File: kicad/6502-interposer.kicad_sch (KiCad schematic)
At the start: 6 parts, among them J1 Conn_02x16_Odd_Even_MountingP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, J2 Conn_02x16_Odd_Even_MountingP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, J3 Conn_02x09_Odd_Even, U1 65CE02

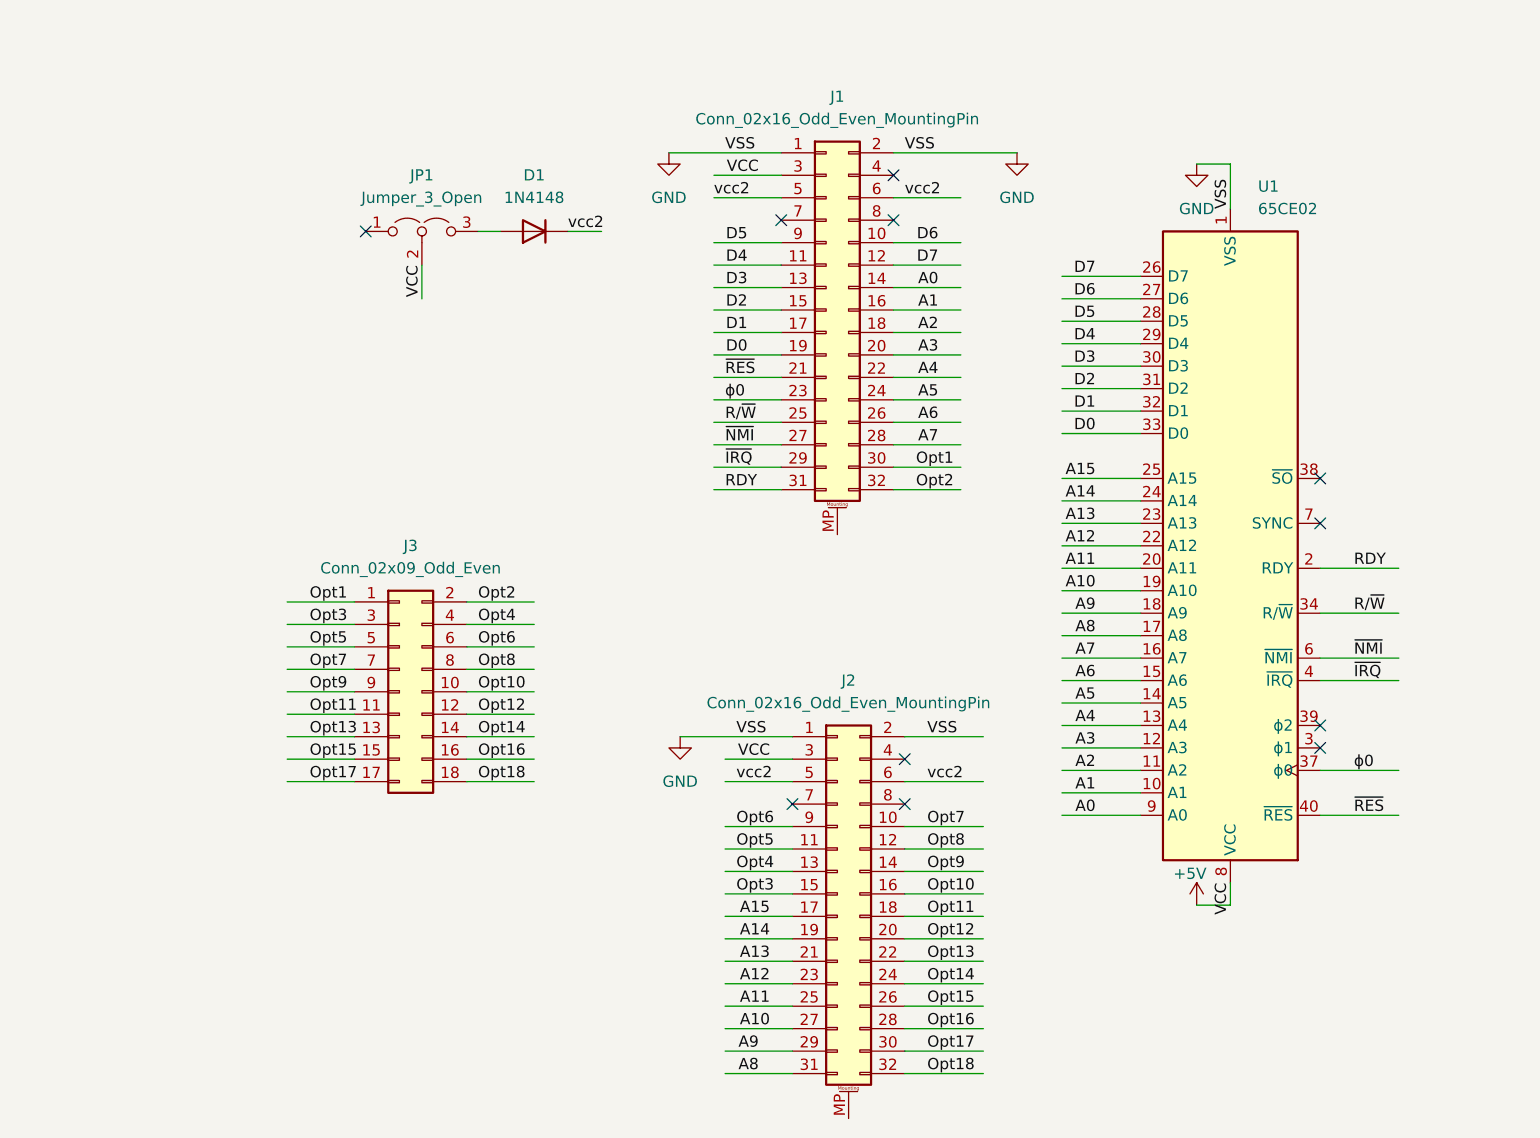
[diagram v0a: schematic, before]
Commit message: version 1.5
Fix board labelling issues. Fix Numbering issues.
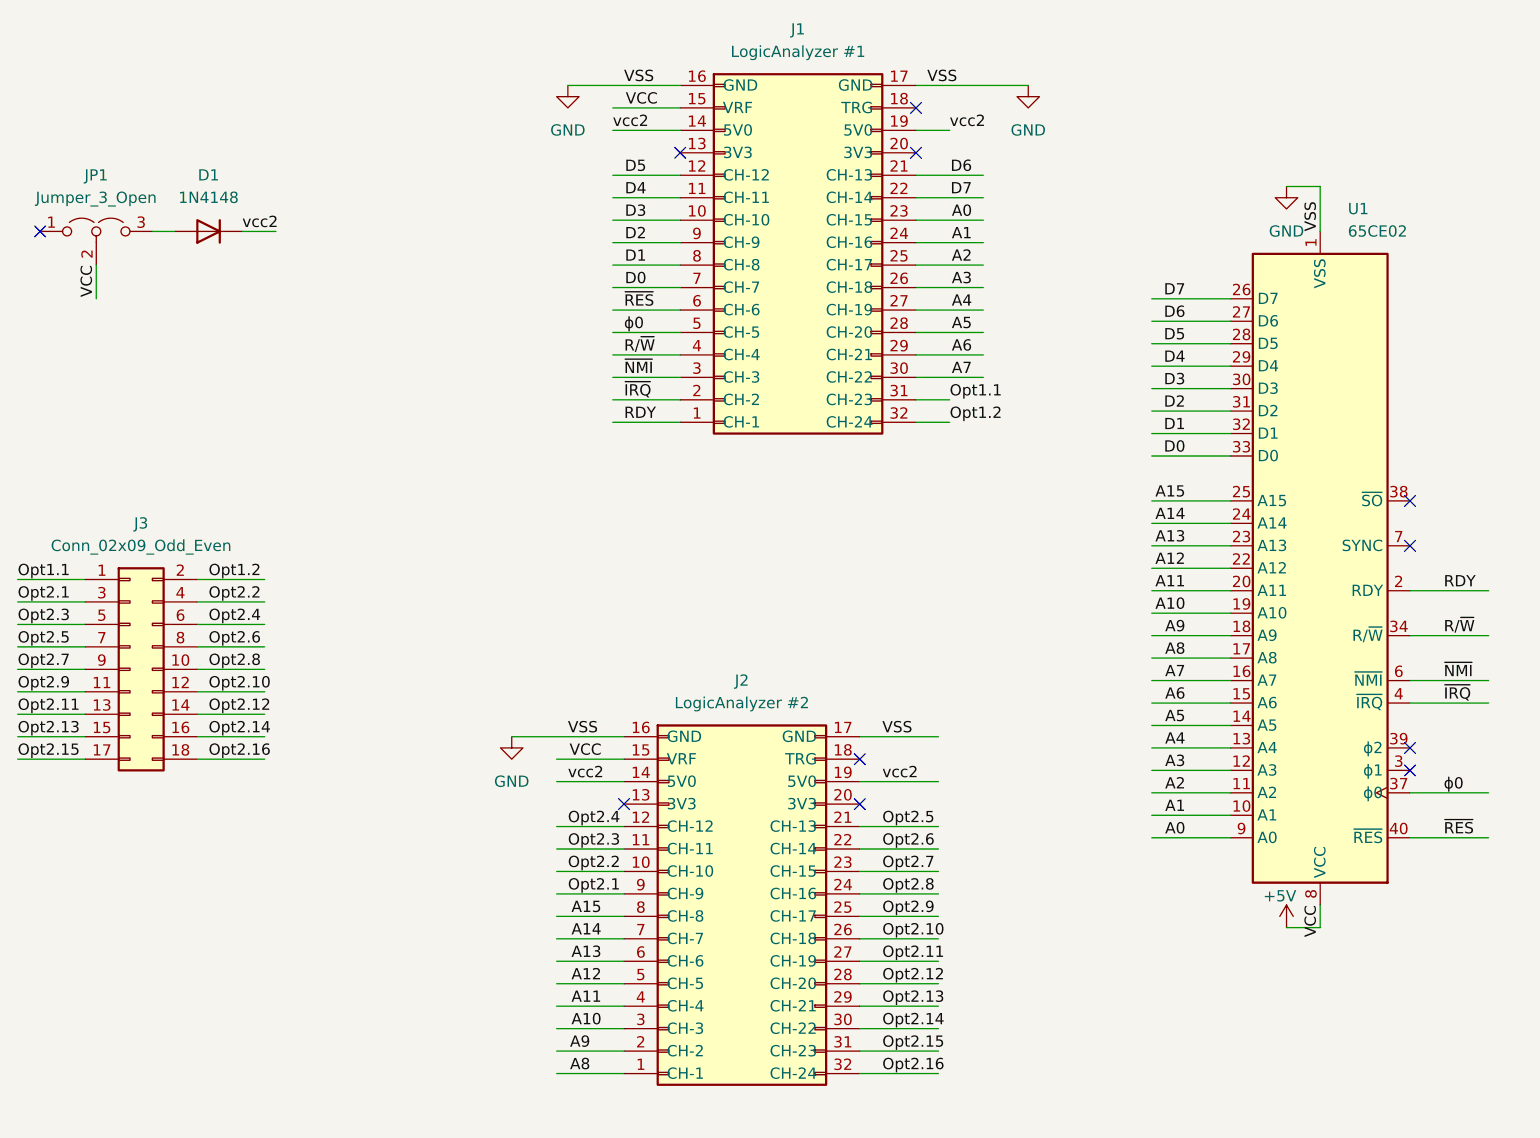
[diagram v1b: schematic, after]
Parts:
- J1: value Conn_02x16_Odd_Even_MountingPin -> LogicAnalyzer #1
- J2: value Conn_02x16_Odd_Even_MountingPin -> LogicAnalyzer #2; symbol Connector_Generic_MountingPin:Conn_02x16_Odd_Even_MountingPin -> LocalLibrary:Dr_Gusman's_Logic_Analyzer_Pinout
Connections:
- net +5V: now also J1.15 (VRF), J2.15 (VRF); no longer J1.3 (Pin_3), J2.3 (Pin_3)
- net A0: now also J1.23 (CH-15); no longer J1.14 (Pin_14)
- net A1: now also J1.24 (CH-16); no longer J1.16 (Pin_16)
- net A10: now also J2.3 (CH-3); no longer J2.27 (Pin_27)
- net A11: now also J2.4 (CH-4); no longer J2.25 (Pin_25)
- net A12: now also J2.5 (CH-5); no longer J2.23 (Pin_23)
- net A13: now also J2.6 (CH-6); no longer J2.21 (Pin_21)
- net A14: now also J2.7 (CH-7); no longer J2.19 (Pin_19)
- net A15: now also J2.8 (CH-8); no longer J2.17 (Pin_17)
- net A2: now also J1.25 (CH-17); no longer J1.18 (Pin_18)
- net A3: now also J1.26 (CH-18); no longer J1.20 (Pin_20)
- net A4: now also J1.27 (CH-19); no longer J1.22 (Pin_22)
- net A5: now also J1.28 (CH-20); no longer J1.24 (Pin_24)
- net A6: now also J1.29 (CH-21); no longer J1.26 (Pin_26)
- net A7: now also J1.30 (CH-22); no longer J1.28 (Pin_28)
- net A8: now also J2.1 (CH-1); no longer J2.31 (Pin_31)
- net A9: now also J2.2 (CH-2); no longer J2.29 (Pin_29)
- net D0: now also J1.7 (CH-7); no longer J1.19 (Pin_19)
- net D1: now also J1.8 (CH-8); no longer J1.17 (Pin_17)
- net D2: now also J1.9 (CH-9); no longer J1.15 (Pin_15)
- net D3: now also J1.10 (CH-10); no longer J1.13 (Pin_13)
- net D5: now also J1.12 (CH-12); no longer J1.9 (Pin_9)
- net D6: now also J1.21 (CH-13); no longer J1.10 (Pin_10)
- net D7: now also J1.22 (CH-14); no longer J1.12 (Pin_12)
- net GND: now also J1.16 (GND), J1.17 (GND), J2.16 (GND), J2.17 (GND); no longer J1.1 (Pin_1), J1.2 (Pin_2), J2.1 (Pin_1), J2.2 (Pin_2)
- net R/~{W}: now also J1.4 (CH-4); no longer J1.25 (Pin_25)
- net RDY: now also J1.1 (CH-1); no longer J1.31 (Pin_31)
- net vcc2: now also J1.14 (5V0), J1.19 (5V0), J2.14 (5V0), J2.19 (5V0); no longer J1.5 (Pin_5), J1.6 (Pin_6), J2.5 (Pin_5), J2.6 (Pin_6)
- net ~{IRQ}: now also J1.2 (CH-2); no longer J1.29 (Pin_29)
- net ~{NMI}: now also J1.3 (CH-3); no longer J1.27 (Pin_27)
- net ~{RES}: now also J1.6 (CH-6); no longer J1.21 (Pin_21)
- net ϕ0: now also J1.5 (CH-5); no longer J1.23 (Pin_23)
- net Opt1 renamed Opt1.1
- net Opt1.1: now also J1.31 (CH-23); no longer J1.30 (Pin_30)
- net Opt10 renamed Opt2.8
- net Opt2.8: now also J2.24 (CH-16); no longer J2.16 (Pin_16)
- net Opt11: no longer names the net of J2.18 (TRG)
- net Opt11: no longer J3.11 (Pin_11)
- net Opt12: no longer names the net of J2.20 (3V3)
- net Opt12: no longer J3.12 (Pin_12)
- net Opt13 renamed Opt2.11
- net Opt2.11: now also J2.27 (CH-19); no longer J2.22 (Pin_22)
- net Opt14 renamed Opt2.12
- net Opt2.12: now also J2.28 (CH-20); no longer J2.24 (Pin_24)
- net Opt15 renamed Opt2.10
- net Opt2.10: now also J3.12 (Pin_12); no longer J3.15 (Pin_15)
- net Opt16 renamed Opt2.14
- net Opt2.14: now also J2.30 (CH-22); no longer J2.28 (Pin_28)
- net Opt17 renamed Opt2.15
- net Opt2.15: now also J2.31 (CH-23); no longer J2.30 (Pin_30)
- net Opt18 renamed Opt2.16
- net Opt2 renamed Opt1.2
- net Opt3 renamed Opt2.1
- net Opt2.1: now also J2.9 (CH-9); no longer J2.15 (Pin_15)
- net Opt4: no longer names the net of J2.13 (3V3)
- net Opt4: no longer J3.4 (Pin_4)
- net Opt5 renamed Opt2.3
- net Opt6 renamed Opt2.4
- net Opt2.4: now also J2.12 (CH-12); no longer J2.9 (Pin_9)
- net Opt7 renamed Opt2.2
- net Opt2.2: now also J3.4 (Pin_4); no longer J3.7 (Pin_7)
- net Opt8 renamed Opt2.6
- net Opt2.6: now also J2.22 (CH-14); no longer J2.12 (Pin_12)
- net Opt9 renamed Opt2.7
- net Opt2.7: now also J2.23 (CH-15); no longer J2.14 (Pin_14)
- new net Opt2.13: J2.29 (CH-21), J3.15 (Pin_15)
- new net Opt2.5: J2.21 (CH-13), J3.7 (Pin_7)
- new net Opt2.9: J2.25 (CH-17), J3.11 (Pin_11)
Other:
- moved on the sheet: D1, J3, JP1, U1

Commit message: repo cleanup and 1.5 update
cleaned up and reorganized the repository. Updated the 1.5 version to latest, hopefully production version.
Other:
- company: (none) -> Ositis
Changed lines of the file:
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@@
 	(title_block
 		(title "6502 interposer")
-		(rev "1.0")
+		(date "2025-09-21")
+		(rev "1.5")
+		(company "Ositis")
+		(comment 1 "https://github.com/eositis/a2-6502-analyzer")
 	)
 	(no_connect
